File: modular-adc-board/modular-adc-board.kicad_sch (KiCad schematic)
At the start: 0 parts

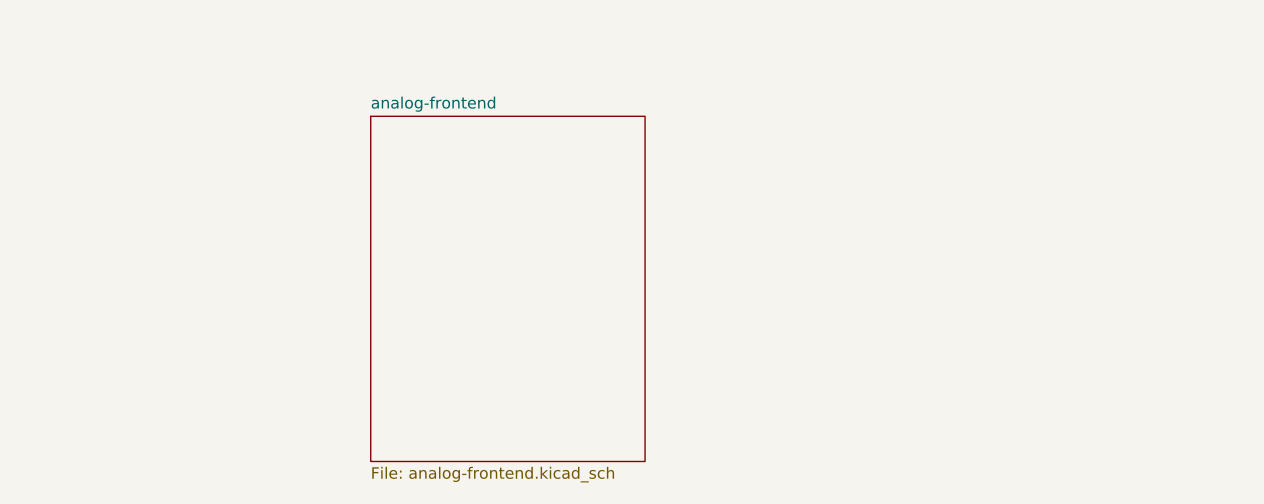
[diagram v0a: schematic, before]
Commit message: minor board changes, notes on double-adc usage, added simulations
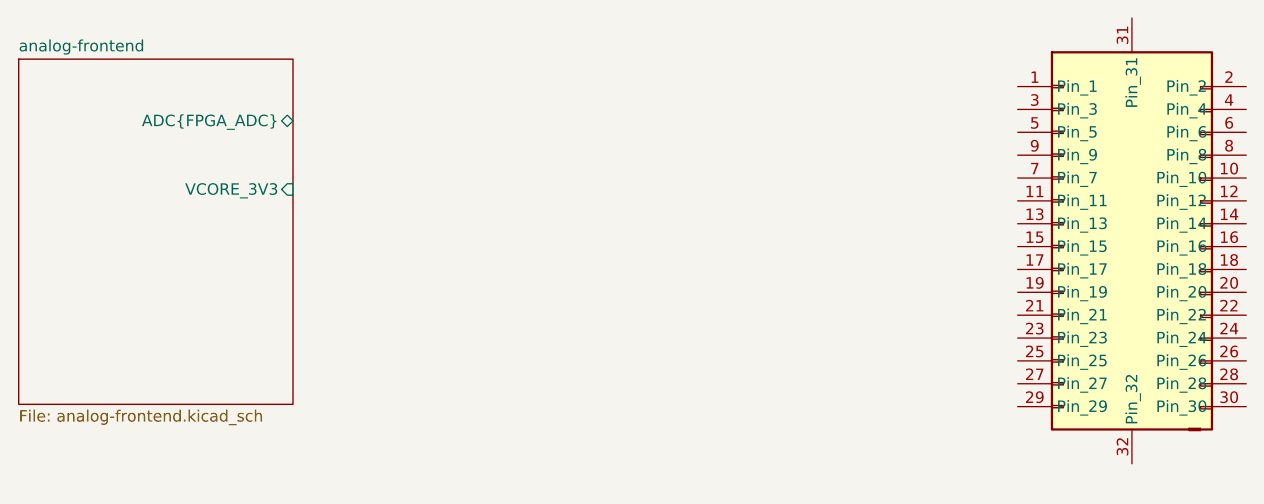
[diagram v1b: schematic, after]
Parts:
- added U101: ~, iw-connector:Hirose_BM28-BM28B0.6-30DP-2-0.35V_2x10_P0.35mm_PowerPin2_Vertical, symbol iw-connector:BM28B0.6-30DP/2-0.35V
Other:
- sheet analog-frontend ports: added ADC{FPGA_ADC}, VCORE_3V3; removed none
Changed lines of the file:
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@@
 	(generator_version "9.0")
 	(paper "A4")
+	(symbol
+		(lib_id "iw-connector:BM28B0.6-30DP/2-0.35V")
+		(at 198.12 86.36 0)
+		(unit 1)
+		(exclude_from_sim no)
+		(in_bom yes)
+		(on_board yes)
+		(dnp no)
+		(fields_autoplaced yes)
+		(property "Reference" "U101"
+			(at 188.976 81.788 0)
+			(effects
+				(font
+					(size 1.27 1.27)
+				)
+				(hide yes)
+			)
+		)
+		(property "Value" "~"
+			(at 200.2633 62.23 0)
+			(effects
+				(font
+					(size 1.27 1.27)
+				)
+				(justify left)
+			)
+		)
+		(property "Footprint" "iw-connector:Hirose_BM28-BM28B0.6-30DP-2-0.35V_2x10_P0.35mm_PowerPin2_Vertical"
+			(at 198.12 86.36 0)
+			(effects
+				(font
+					(size 1.27 1.27)
+				)
+				(hide yes)
+			)
+		)
+		(property "Datasheet" "https://jlcpcb.com/api/file/downloadByFileSystemAccessId/8588911873114300416"
+			(at 198.12 86.36 0)
+			(effects
+				(font
+					(size 1.27 1.27)
+				)
+				(hide yes)
+			)
+		)
+		(property "Description" ""
+			(at 198.12 86.36 0)
+			(effects
+				(font
+					(size 1.27 1.27)
+				)
+				(hide yes)
+			)
+		)
+		(property "MPN" "BM28B0.6-30DP/2-0.35V(51) "
+			(at 198.12 86.36 0)
+			(effects
+				(font
+					(size 1.27 1.27)
+				)
+				(hide yes)
+			)
+		)
+		(property "LPN" "C424570"
+			(at 198.12 86.36 0)
+			(effects
+				(font
+					(size 1.27 1.27)
+				)
+				(hide yes)
+			)
+		)
+		(pin "4"
+		)
+		(pin "12"
+		)
+		(pin "32"
+		)
+		(pin "14"
+		)
+		(pin "18"
+		)
+		(pin "19"
+		)
+		(pin "27"
+		)
+		(pin "6"
+		)
+		(pin "2"
+		)
+		(pin "31"
+		)
+		(pin "1"
+		)
+		(pin "20"
+		)
+		(pin "8"
+		)
+		(pin "24"
+		)
+		(pin "29"
+		)
+		(pin "16"
+		)
+		(pin "26"
+		)
+		(pin "25"
+		)
+		(pin "3"
+		)
+		(pin "5"
+		)
+		(pin "9"
+		)
+		(pin "11"
+		)
+		(pin "7"
+		)
+		(pin "13"
+		)
+		(pin "10"
+		)
+		(pin "22"
+		)
+		(pin "28"
+		)
+		(pin "21"
+		)
+		(pin "30"
+		)
+		(pin "15"
+		)
+		(pin "17"
+		)
+		(pin "23"
+		)
+		(instances
+			(project ""
+				(path "/3e298956-65b1-40d9-b81f-ffb699dde4c7"
+					(reference "U101")
+					(unit 1)
+				)
+			)
+		)
+	)
 	(sheet
-		(at 113.538 71.882)
+		(at 74.422 65.532)
 		(size 30.48 38.354)
 		(exclude_from_sim no)
@@
 		)
 		(property "Sheetname" "analog-frontend"
-			(at 113.538 71.1704 0)
+			(at 74.422 64.8204 0)
 			(effects
 				(font
@@
 		)
 		(property "Sheetfile" "analog-frontend.kicad_sch"
-			(at 113.538 110.8206 0)
+			(at 74.422 104.4706 0)
 			(effects
 				(font
@@
 			)
 		)
+		(pin "ADC{FPGA_ADC}" bidirectional
+			(at 104.902 72.39 0)
+			(effects
+				(font
+					(size 1.27 1.27)
+				)
+				(justify right)
+			)
+		)
+		(pin "VCORE_3V3" input
+			(at 104.902 80.01 0)
+			(effects
+				(font
+					(size 1.27 1.27)
+				)
+				(justify right)
+			)
+		)
